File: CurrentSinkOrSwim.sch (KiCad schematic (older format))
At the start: 3 parts, among them P101 CONN_01X02, P102 CONN_01X03, P103 CONN_01X02

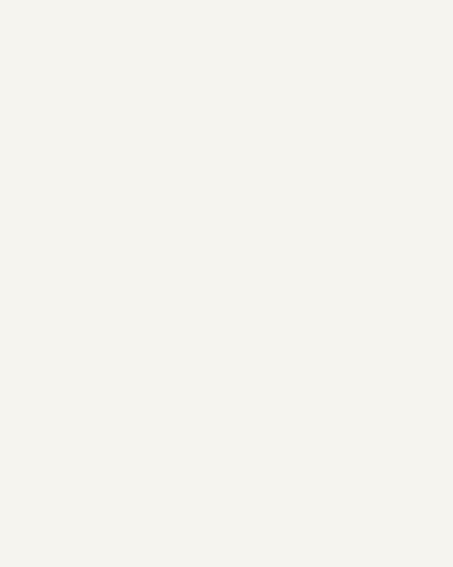
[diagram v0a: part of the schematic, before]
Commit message: added measure pins and ripup layout
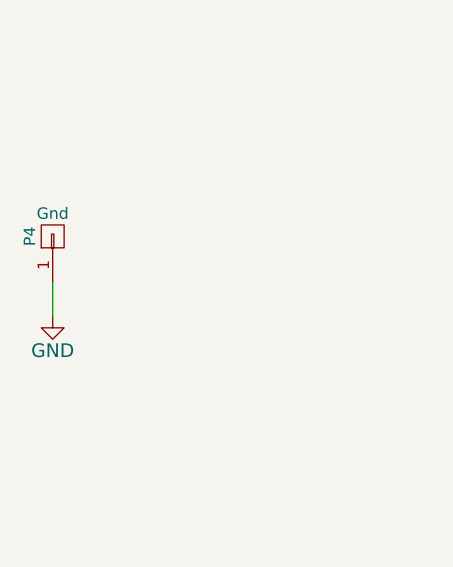
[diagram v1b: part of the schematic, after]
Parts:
- added P4: Gnd, symbol CONN_01X01
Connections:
- net GND: now also P4.1 (P1)
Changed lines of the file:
@@
 $EndComp
 $Comp
-L GND #PWR01
+L GND #PWR1
 U 1 1 54D85A15
 P 3350 1450
-F 0 "#PWR01" H 3350 1200 60  0001 C CNN
+F 0 "#PWR1" H 3350 1200 60  0001 C CNN
 F 1 "GND" H 3350 1300 60  0000 C CNN
 F 2 "" H 3350 1450 60  0000 C CNN
@@
 	4550 4400 4800 4400
 $Comp
-L GND #PWR02
+L GND #PWR3
 U 1 1 54DB4AD2
 P 7900 6250
-F 0 "#PWR02" H 7900 6000 60  0001 C CNN
+F 0 "#PWR3" H 7900 6000 60  0001 C CNN
 F 1 "GND" H 7900 6100 60  0000 C CNN
 F 2 "" H 7900 6250 60  0000 C CNN
@@
 	6500 6000 7900 6000
 Connection ~ 7900 6000
+$Comp
+L CONN_01X01 P4
+U 1 1 54F1F73D
+P 2200 4000
+F 0 "P4" H 2200 4100 50  0000 C CNN
+F 1 "Gnd" V 2300 4000 50  0000 C CNN
+F 2 "" H 2200 4000 60  0000 C CNN
+F 3 "" H 2200 4000 60  0000 C CNN
+	1    2200 4000
+	0    -1   -1   0
+$EndComp
+$Comp
+L GND #PWR2
+U 1 1 54F1F7D2
+P 2200 4350
+F 0 "#PWR2" H 2200 4100 60  0001 C CNN
+F 1 "GND" H 2200 4200 60  0000 C CNN
+F 2 "" H 2200 4350 60  0000 C CNN
+F 3 "" H 2200 4350 60  0000 C CNN
+	1    2200 4350
+	1    0    0    -1
+$EndComp
+Wire Wire Line
+	2200 4200 2200 4350
 $EndSCHEMATC
